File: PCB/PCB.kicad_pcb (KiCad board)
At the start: 2 copper layers, 80 x 100 mm, 115 parts, among them J1 External Trig, J3 Conn_Coaxial, J4 RJ12, J5 Programming Header, J6 Camera TRS, J7 Conn_Coaxial, J8 USB_C_Receptacle_USB2.0_14P, Q3 MMBF170, Q4 MMBF170, Q5 FDN340P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

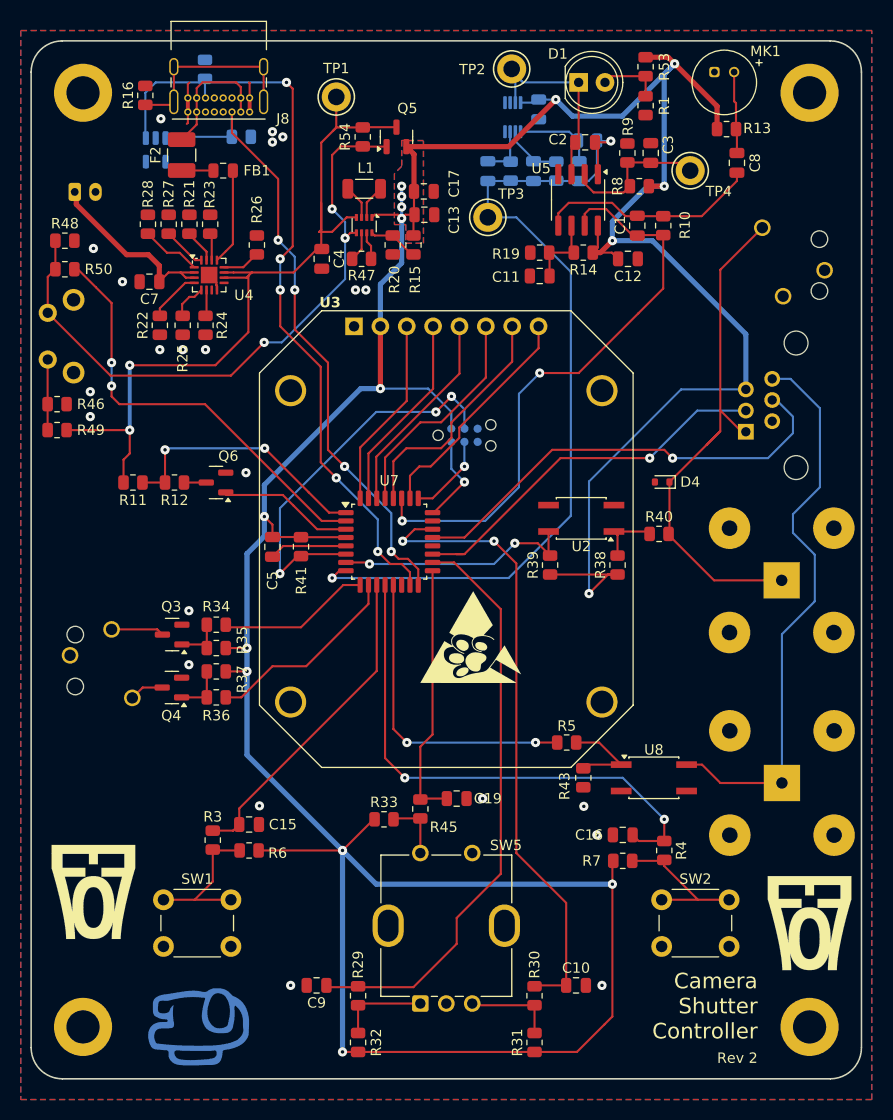
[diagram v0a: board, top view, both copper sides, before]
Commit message: Rev 2 of the PCB with modified test firmware and enclosure
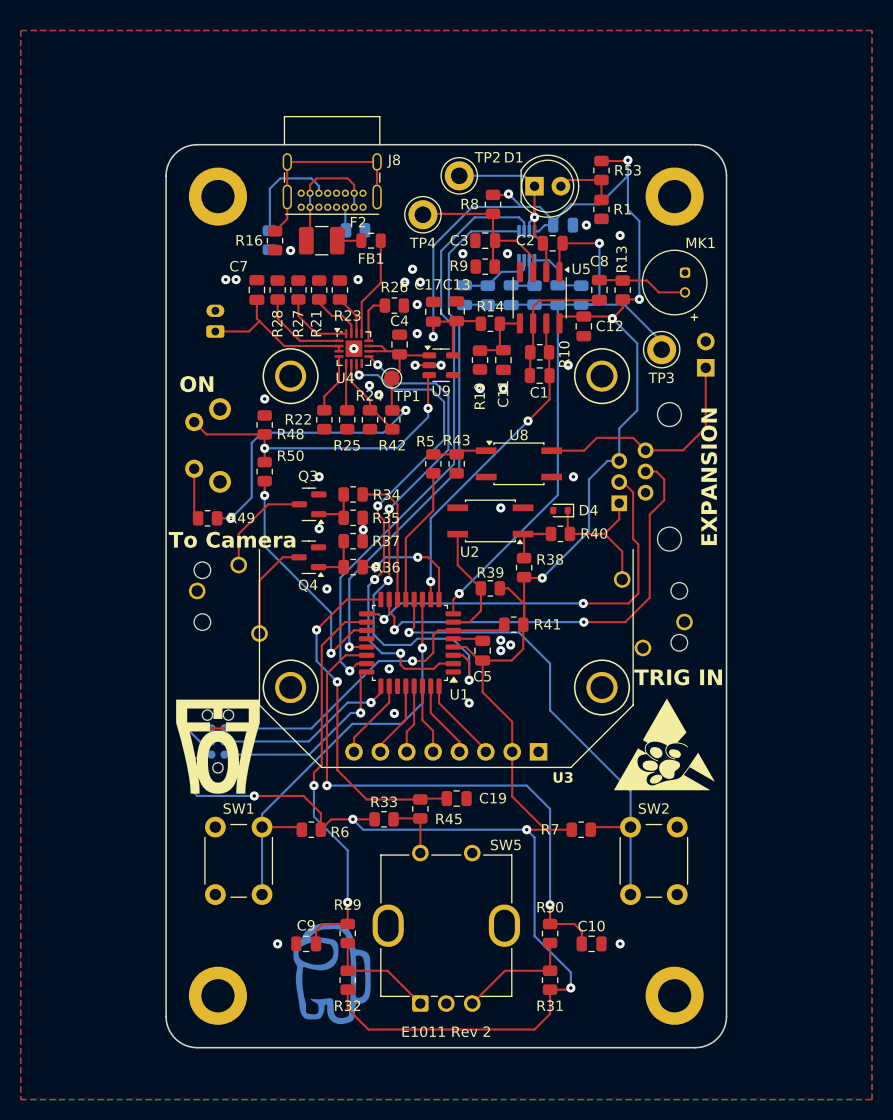
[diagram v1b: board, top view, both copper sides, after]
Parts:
- removed C15, C16: 10nF, Capacitor_SMD:C_0805_2012Metric
- removed D2: ESDA14V2SC5, Package_TO_SOT_SMD:SOT-23-5
- removed the G*** at (36.0, 109.0)
- removed J3, J7: Conn_Coaxial, Connector_Coaxial:BNC_TEConnectivity_1478035_Horizontal
- removed L1: L, Inductor_SMD:L_1206_3216Metric
- removed Q5: FDN340P, Package_TO_SOT_SMD:SOT-23
- removed Q6: MMBF170, Package_TO_SOT_SMD:SOT-23
- removed R11, R12: 100k, Resistor_SMD:R_0805_2012Metric
- removed R15: 56k, Resistor_SMD:R_0805_2012Metric
- removed R20, R54: 10k, Resistor_SMD:R_0805_2012Metric
- removed R3, R4, R46: 1k, Resistor_SMD:R_0805_2012Metric
- removed R47: 0, Resistor_SMD:R_0805_2012Metric
- removed U7: STM32G071K8Tx, Package_QFP:LQFP-32_7x7mm_P0.8mm
- added J2: Conn_01x02_Socket, Connector_PinHeader_2.54mm:PinHeader_1x02_P2.54mm_Vertical, B.Cu at (95.0, 58.5)
- added R42: 1k, Resistor_SMD:R_0805_2012Metric, F.Cu at (64.8, 63.5)
- added U9: TLV75733PDBV, Package_TO_SOT_SMD:SOT-23-5, F.Cu at (69.5, 58.2)
- C13: value 47uF -> 10uF
- C4: value 22uF -> 10uF
- R24: value 10k -> 0
- R25: value 10k -> 1k
- TP1: footprint TestPoint:TestPoint_Keystone_5005-5009_Compact -> TestPoint:TestPoint_Pad_D1.5mm
- U1: value TPS631000 -> STM32G071K8Tx; footprint Package_TO_SOT_SMD:SOT-583-8 -> Package_QFP:LQFP-32_7x7mm_P0.8mm
- moved G*** 59.5 mm to (48.0, 95.0)
- moved U3 44.7 mm to (78.9, 95.5), turned to 180 degrees
- moved U1 40.5 mm to (66.5, 85.0), turned to 180 degrees
- moved J5 37.9 mm to (48.0, 94.5), turned to 90 degrees
- moved J1 36.5 mm to (96.5, 83.0)
- moved G*** 34.1 mm to (70.0, 112.0)
- moved U8 32.9 mm to (77.0, 67.8)
- moved R43 32.6 mm to (71.0, 67.8)
- moved R5 29.8 mm to (68.8, 67.8), turned to 90 degrees
- moved TP1 27.6 mm to (64.8, 59.5)
- moved R50 27.4 mm to (52.5, 68.5), turned to 90 degrees
- moved R48 26.2 mm to (52.5, 64.0), turned to 90 degrees
- moved TP4 26.1 mm to (67.8, 43.8)
- moved C5 22.6 mm to (73.5, 85.8), turned to 90 degrees
- moved R41 21.8 mm to (76.5, 83.2), turned to 180 degrees
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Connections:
- net /BATT-EN1 renamed Net-(U4-EN1)
- net /BATT-EN2 renamed Net-(U4-EN2)
- net /CC1 renamed Net-(J8-CC1)
- net /CC2 renamed Net-(J8-CC2)
- C1 pad 1: Net-(U5B-+) -> Net-(U5B--)
- C11 pad 2: Net-(U5B--) -> Net-(U5B-+)
- C3 pad 2: Net-(U5A--) -> Net-(U5A-+)
- C8 pad 2: Net-(U5B-+) -> Net-(U5B--)
- R10 pad 2: Net-(U5B-+) -> Net-(U5B--)
- R14 pad 2: Net-(U5B--) -> Net-(U5B-+)
- R19 pad 2: Net-(U5B--) -> Net-(U5B-+)
- R35 pad 1: Net-(Q3-G) -> GND
- R35 pad 2: +3.3V -> Net-(Q3-G)
- R37 pad 1: Net-(Q4-G) -> GND
- R37 pad 2: +3.3V -> Net-(Q4-G)
- R6 pad 2: Net-(R3-Pad2) -> /BT1
- R7 pad 2: Net-(R4-Pad2) -> /BT2
- R8 pad 2: Net-(U5A--) -> Net-(U5A-+)
- R9 pad 2: Net-(U5A--) -> Net-(U5A-+)
- SW1 pad 1: Net-(R3-Pad2) -> /BT1
- SW2 pad 1: Net-(R4-Pad2) -> /BT2
- TP4 pad 1: Net-(U5A--) -> Net-(U5A-+)
- U1 pad 1: +3.3V -> unconnected-(U1-PB9-Pad1)
- U1 pad 2: Net-(U1-LX2) -> /~{PGOOD}
- U1 pad 3: Net-(U1-LX1) -> /~{CHR}
- U1 pad 4: /BATT-OUT -> +3.3V
- U1 pad 5: /3V3_EN -> GND
- U1 pad 6: Net-(U1-MODE) -> /PROG_RST
- U1 pad 7: GND -> /EXT_TRIG_IN
- U1 pad 8: Net-(U1-FB) -> /LIGHT_DEC
- U5 pad 2: Net-(U5A--) -> Net-(D1-K)
- U5 pad 3: Net-(D1-K) -> Net-(U5A-+)
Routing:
- net +3.3V: track 349.8 -> 235.6 mm, vias 16 -> 10
- net Net-(J8-CC2): track 76.0 -> 10.2 mm, vias 5 -> 0
- net Net-(J8-CC1): track 62.4 -> 2.25 mm, vias 4 -> 0
- net /TIA_SEL1: track 0.00 -> 58.2 mm, vias 0 -> 1
- net /TIA_SEL2: track 0.00 -> 52.0 mm, vias 0 -> 1
- net /~{CHR}: track 0.00 -> 51.7 mm, vias 0 -> 4
- net /~{PGOOD}: track 0.00 -> 47.1 mm, vias 0 -> 4
- net /EXT_TRIG_{IN}: track 51.6 -> 14.3 mm
- net /BATT-OUT: track 77.3 -> 40.5 mm
- net /TRG_{OUT}_{1}: track 55.1 -> 22.5 mm
- net /3V3_EN: track 61.6 -> 31.0 mm, vias 3 -> 2
- net /AUDIO_DEC: track 57.0 -> 31.5 mm
- net /BATT_MON: track 25.4 -> 0.00 mm, vias 2 -> 0
- net /ROT_A: track 56.8 -> 38.3 mm, vias 0 -> 2
- net /3V3_EN_MCU: track 41.5 -> 23.6 mm
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- removed copper zone on B.Cu, net +3.3V
- removed copper zone on F.Cu, net +3.3V
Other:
- board size 80 x 100 mm -> 54 x 87 mm
- rule pad_to_mask_clearance: 0 -> 0.1016
- board text added: "E1011 Camera Shutter Controller Rev 2"
- board text added: "E1011 Rev 2"
- board text removed: "Camera Shutter Controller"
- board text removed: "Camera Shutter Controller Rev 2"
- board text removed: "Rev 2"
- board text removed: "TRIG OUT"
